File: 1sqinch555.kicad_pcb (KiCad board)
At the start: 2 copper layers, 104.5 x 25 mm, 75 parts, among them J1 Conn_01x01, J10 Conn_01x01, J11 Conn_01x01, J12 Conn_01x01, J13 Conn_01x01, J14 Conn_01x01, J15 Conn_01x01, J16 Conn_01x01, J17 Conn_01x01, J18 Conn_01x01, J19 Conn_01x01, J2 Conn_01x01, J20 Conn_01x01, J21 Conn_01x01, J22 Conn_01x01, J23 Conn_01x01, J24 Conn_01x01, J25 Conn_01x01, J26 Conn_01x01, J27 Conn_01x01, J28 Conn_01x01, J29 Conn_01x01, J3 Conn_01x01, J30 Conn_01x01, J31 Conn_01x01, J32 Conn_01x01, J33 Conn_01x01, J34 Conn_01x01, J35 Conn_01x01, J4 Conn_01x01, J5 Conn_01x01, J6 Conn_01x01, J7 Conn_01x01, J8 Conn_01x01, J9 Conn_01x01, U1 LM555, U2 4020

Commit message: changed 0603 to 0805
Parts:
- added R10: 300, 1sqinch555_fp:R_0805, F.Cu at (137.7, 38.5)
- added R2: 300, 1sqinch555_fp:R_0805, F.Cu at (69.4, 38.5)
- added R3: 300, 1sqinch555_fp:R_0805, F.Cu at (73.8, 38.5)
- added R4: 300, 1sqinch555_fp:R_0805, F.Cu at (84.6, 38.5)
- added R5: 300, 1sqinch555_fp:R_0805, F.Cu at (95.9, 38.5)
- added R6: 300, 1sqinch555_fp:R_0805, F.Cu at (100.3, 38.5)
- added R7: 300, 1sqinch555_fp:R_0805, F.Cu at (111.1, 38.5)
- added R8: 300, 1sqinch555_fp:R_0805, F.Cu at (122.3, 38.5)
- added R9: 300, 1sqinch555_fp:R_0805, F.Cu at (126.9, 38.5)
- C1, C2: footprint 1sqinch555_fp:C_0603 -> 1sqinch555_fp:C_0805
- D1, D10, D11, D12, D13, D14, D15, D16, D17, D18, D19, D2, D20, D21, D22, D23, D24, D25, D26, D27, D3, D4, D5, D6, D7, D8, D9: footprint 1sqinch555_fp:D_0603 -> 1sqinch555_fp:LED-0805
- R1: footprint 1sqinch555_fp:R_0603 -> 1sqinch555_fp:R_0805
- moved J30 1.50 mm to (71.5, 41.0)
- moved J31 1.50 mm to (82.5, 41.0)
- moved J32 1.50 mm to (98.0, 41.0)
- moved J33 1.50 mm to (109.0, 41.0)
- moved J34 1.50 mm to (135.5, 41.0)
- moved J35 1.50 mm to (124.5, 41.0)
- moved C1 0.51 mm to (55.5, 60.6)
- moved R1 0.51 mm to (53.0, 60.6)
- moved D11 0.20 mm to (92.7, 47.5)
- moved D17 0.20 mm to (114.3, 47.5)
- moved D2 0.20 mm to (66.2, 47.5)
- moved D20 0.20 mm to (119.2, 47.5)
- moved D8 0.20 mm to (87.8, 47.5)
- moved D26 0.20 mm to (140.8, 47.5)
- moved D1 0.20 mm to (66.2, 55.5)
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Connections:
- D12 pad 1: /GND2 -> Net-(D12-Pad1)
- D15 pad 1: /GND2 -> Net-(D15-Pad1)
- D18 pad 1: /GND2 -> Net-(D18-Pad1)
- D21 pad 1: /GND3 -> Net-(D21-Pad1)
- D24 pad 1: /GND3 -> Net-(D24-Pad1)
- D27 pad 1: /GND3 -> Net-(D27-Pad1)
- D3 pad 1: /GND1 -> Net-(D3-Pad1)
- D6 pad 1: /GND1 -> Net-(D6-Pad1)
- D9 pad 1: /GND1 -> Net-(D9-Pad1)
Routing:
- net /GND3: track 63.4 -> 0.00 mm
- net /GND1: track 63.4 -> 0.00 mm
- net /GND2: track 63.4 -> 0.00 mm
- net /GND: track 16.4 -> 4.62 mm
- net Net-(D8-Pad1): track 6.30 -> 0.00 mm
- net Net-(D7-Pad1): track 6.30 -> 0.00 mm
- net Net-(D26-Pad1): track 6.30 -> 0.00 mm
- net Net-(D25-Pad1): track 6.30 -> 0.00 mm
- net Net-(D20-Pad1): track 6.30 -> 0.00 mm
- net Net-(D2-Pad1): track 6.30 -> 0.00 mm
- net Net-(D19-Pad1): track 6.30 -> 0.00 mm
- net Net-(D17-Pad1): track 6.30 -> 0.00 mm
- net Net-(D16-Pad1): track 6.30 -> 0.00 mm
- net Net-(D11-Pad1): track 6.30 -> 0.00 mm
- net Net-(D10-Pad1): track 6.30 -> 0.00 mm
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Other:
- outline, holes or cut-outs redrawn

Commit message: layout changes
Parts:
- moved C1 11.0 mm to (46.0, 55.0)
- moved R1 11.0 mm to (43.5, 55.0), turned to 90 degrees
- moved G1 4.73 mm to (36.5, 41.6), turned to 0 degrees
- moved C2 1.04 mm to (57.7, 59.6), turned to 180 degrees
- moved J3 0.83 mm to (51.2, 47.5)
- moved J1 0.81 mm to (60.5, 54.5)
- moved U1 0.80 mm to (56.0, 55.2)
- moved R8 0.11 mm to (122.4, 38.5)
- moved R9 0.11 mm to (126.8, 38.5)
- moved R10 0.11 mm to (137.6, 38.5)
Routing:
- net /GND: track 4.62 -> 66.9 mm, vias 6 -> 7
- net /GND3: track 0.00 -> 41.3 mm, vias 0 -> 1
- net /GND2: track 0.00 -> 41.3 mm, vias 0 -> 1
- net /GND1: track 0.00 -> 41.3 mm, vias 0 -> 1
- net /OUT: track 17.9 -> 28.2 mm
- net /Q13: track 28.2 -> 37.6 mm
- net Net-(D8-Pad1): track 0.00 -> 5.90 mm
- net Net-(D7-Pad1): track 0.00 -> 5.90 mm
- net Net-(D5-Pad1): track 0.00 -> 5.90 mm
- net Net-(D4-Pad1): track 0.00 -> 5.90 mm
- net Net-(D26-Pad1): track 0.00 -> 5.90 mm
- net Net-(D25-Pad1): track 0.00 -> 5.90 mm
- net Net-(D23-Pad1): track 0.00 -> 5.90 mm
- net Net-(D22-Pad1): track 0.00 -> 5.90 mm
- net Net-(D20-Pad1): track 0.00 -> 5.90 mm
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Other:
- outline, holes or cut-outs redrawn
- board text added: "1sqinch555"

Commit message: mods
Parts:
- removed mouse-bite-2.5mm-slot (x6): VAL**, 1sqinch555_fp:mouse-bite-2.5mm-slot
- moved D19 4.50 mm to (114.7, 55.5)
- moved D20 4.50 mm to (114.7, 47.5)
- moved D21 4.50 mm to (114.7, 39.5)
- moved D22 4.50 mm to (125.5, 55.5)
- moved D23 4.50 mm to (125.5, 47.5)
- moved D24 4.50 mm to (125.5, 39.5)
- moved D25 4.50 mm to (136.3, 55.5)
- moved D26 4.50 mm to (136.3, 47.5)
- moved D27 4.50 mm to (136.3, 39.5)
- moved J19 4.50 mm to (114.5, 59.5)
- moved J21 4.50 mm to (125.5, 59.5)
- moved J23 4.50 mm to (136.5, 59.5)
- moved J29 4.50 mm to (131.0, 59.5)
- moved J34 4.50 mm to (131.0, 41.0)
- moved J35 4.50 mm to (120.0, 41.0)
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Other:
- board size 104.5 x 25 mm -> 100 x 25 mm

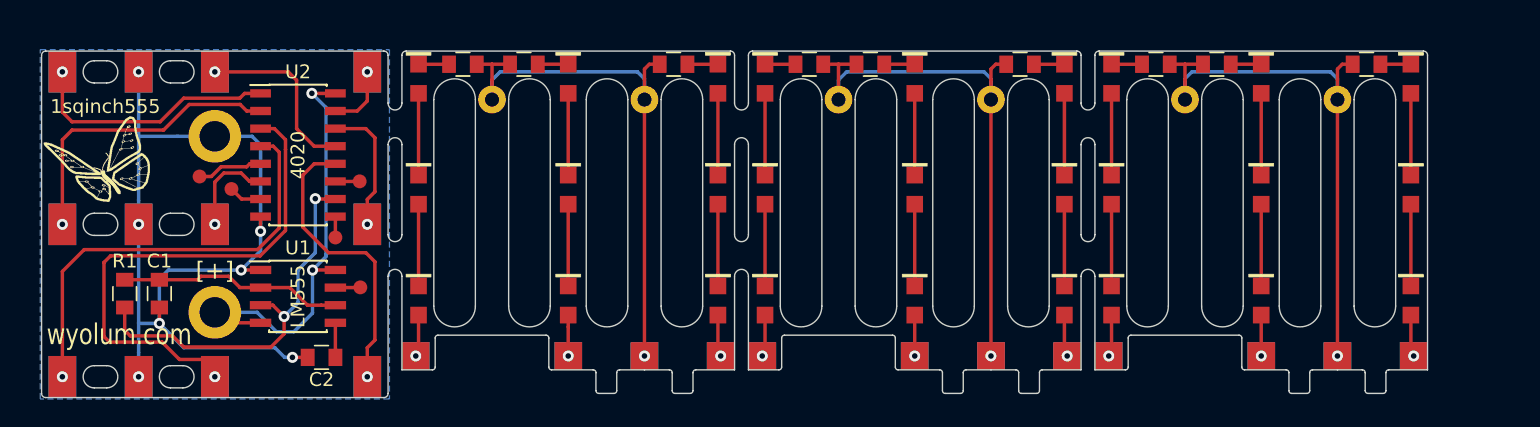
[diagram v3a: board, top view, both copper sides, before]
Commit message: randomizing LEDs
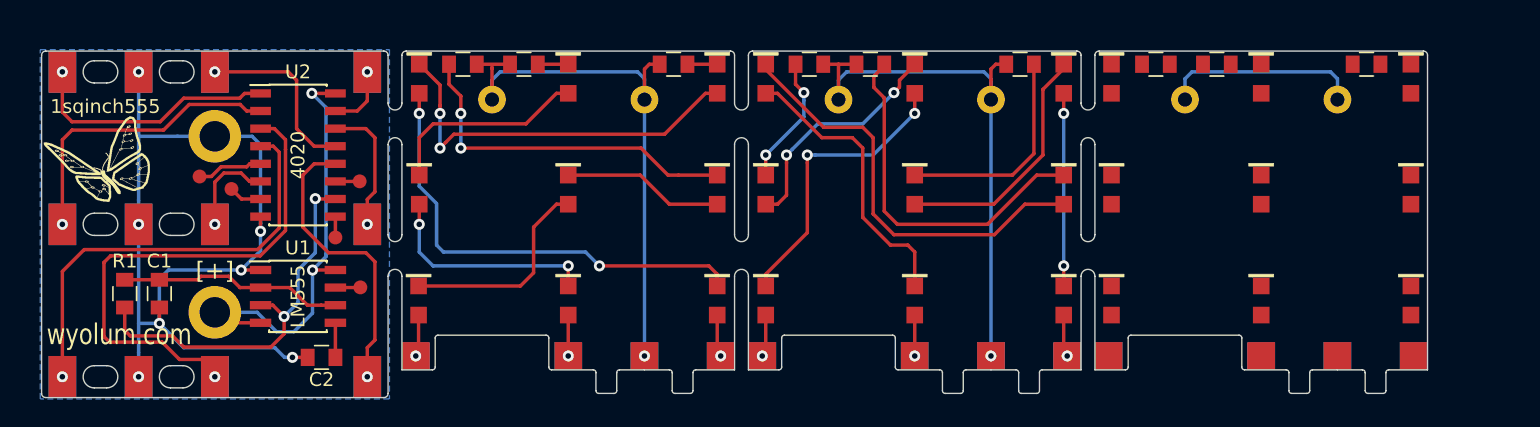
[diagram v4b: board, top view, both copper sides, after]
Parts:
- moved D3 23.0 mm to (86.2, 47.5)
- moved D8 23.0 mm to (64.8, 39.5)
- moved D11 13.4 mm to (100.5, 39.5)
- moved D18 13.4 mm to (100.5, 47.5)
- moved D14 13.4 mm to (89.8, 39.5)
- moved D15 13.4 mm to (111.2, 47.5)
- moved D2 10.8 mm to (75.5, 47.5)
- moved D5 10.8 mm to (64.8, 47.5)
- moved D12 8.00 mm to (89.8, 47.5)
- moved D17 8.00 mm to (111.2, 39.5)
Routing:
- net Net-(D7-Pad1): track 5.90 -> 33.4 mm, vias 0 -> 2
- net /GND3: track 41.3 -> 14.4 mm, vias 1 -> 0
- net Net-(D14-Pad1): track 5.90 -> 30.9 mm
- net Net-(D15-Pad1): track 2.20 -> 26.0 mm
- net Net-(D3-Pad1): track 2.20 -> 25.7 mm, vias 0 -> 2
- net Net-(D8-Pad1): track 5.90 -> 28.3 mm, vias 0 -> 2
- net Net-(D10-Pad1): track 5.90 -> 21.1 mm, vias 0 -> 2
- net Net-(D13-Pad1): track 5.90 -> 20.9 mm
- net Net-(D18-Pad1): track 2.20 -> 15.7 mm
- net Net-(D17-Pad1): track 5.90 -> 17.9 mm
- net Net-(D11-Pad1): track 5.90 -> 17.0 mm, vias 0 -> 2
- net Net-(D4-Pad1): track 5.90 -> 16.1 mm, vias 0 -> 2
- net Net-(D1-Pad1): track 5.90 -> 15.2 mm
- net Net-(D5-Pad1): track 5.90 -> 14.8 mm
- net Net-(D16-Pad1): track 5.90 -> 13.9 mm, vias 0 -> 2
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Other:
- outline, holes or cut-outs redrawn

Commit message: 1mm PCB thickness
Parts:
- added REF**: Unplated_Hole_d1.0mm, 1sqinch555_fp:Unplated_Hole_d1.0mm, F.Cu at (63.0, 51.0)
- added REF**: Unplated_Hole_d1.0mm, 1sqinch555_fp:Unplated_Hole_d1.0mm, F.Cu at (63.0, 57.0)
- added REF**: Unplated_Hole_d1.0mm, 1sqinch555_fp:Unplated_Hole_d1.0mm, F.Cu at (88.0, 39.0)
- added REF**: Unplated_Hole_d1.0mm, 1sqinch555_fp:Unplated_Hole_d1.0mm, F.Cu at (88.0, 41.0)
- added REF**: Unplated_Hole_d1.0mm, 1sqinch555_fp:Unplated_Hole_d1.0mm, F.Cu at (88.0, 43.0)
- added REF**: Unplated_Hole_d1.0mm, 1sqinch555_fp:Unplated_Hole_d1.0mm, F.Cu at (88.0, 45.0)
- added REF**: Unplated_Hole_d1.0mm, 1sqinch555_fp:Unplated_Hole_d1.0mm, F.Cu at (88.0, 47.0)
- added REF**: Unplated_Hole_d1.0mm, 1sqinch555_fp:Unplated_Hole_d1.0mm, F.Cu at (88.0, 49.0)
- added REF**: Unplated_Hole_d1.0mm, 1sqinch555_fp:Unplated_Hole_d1.0mm, F.Cu at (88.0, 51.0)
- added REF**: Unplated_Hole_d1.0mm, 1sqinch555_fp:Unplated_Hole_d1.0mm, F.Cu at (88.0, 53.0)
- added REF**: Unplated_Hole_d1.0mm, 1sqinch555_fp:Unplated_Hole_d1.0mm, F.Cu at (88.0, 55.0)
- added REF**: Unplated_Hole_d1.0mm, 1sqinch555_fp:Unplated_Hole_d1.0mm, F.Cu at (63.0, 39.0)
- added REF**: Unplated_Hole_d1.0mm, 1sqinch555_fp:Unplated_Hole_d1.0mm, F.Cu at (88.0, 57.0)
- added REF**: Unplated_Hole_d1.0mm, 1sqinch555_fp:Unplated_Hole_d1.0mm, F.Cu at (113.0, 39.0)
- added REF**: Unplated_Hole_d1.0mm, 1sqinch555_fp:Unplated_Hole_d1.0mm, F.Cu at (113.0, 41.0)
- added REF**: Unplated_Hole_d1.0mm, 1sqinch555_fp:Unplated_Hole_d1.0mm, F.Cu at (113.0, 43.0)
- added REF**: Unplated_Hole_d1.0mm, 1sqinch555_fp:Unplated_Hole_d1.0mm, F.Cu at (113.0, 45.0)
- added REF**: Unplated_Hole_d1.0mm, 1sqinch555_fp:Unplated_Hole_d1.0mm, F.Cu at (113.0, 47.0)
- added REF**: Unplated_Hole_d1.0mm, 1sqinch555_fp:Unplated_Hole_d1.0mm, F.Cu at (113.0, 49.0)
- added REF**: Unplated_Hole_d1.0mm, 1sqinch555_fp:Unplated_Hole_d1.0mm, F.Cu at (113.0, 51.0)
- added REF**: Unplated_Hole_d1.0mm, 1sqinch555_fp:Unplated_Hole_d1.0mm, F.Cu at (113.0, 53.0)
- added REF**: Unplated_Hole_d1.0mm, 1sqinch555_fp:Unplated_Hole_d1.0mm, F.Cu at (113.0, 55.0)
- added REF**: Unplated_Hole_d1.0mm, 1sqinch555_fp:Unplated_Hole_d1.0mm, F.Cu at (63.0, 41.0)
- added REF**: Unplated_Hole_d1.0mm, 1sqinch555_fp:Unplated_Hole_d1.0mm, F.Cu at (113.0, 57.0)
- added REF**: Unplated_Hole_d1.0mm, 1sqinch555_fp:Unplated_Hole_d1.0mm, F.Cu at (63.0, 43.0)
- added REF**: Unplated_Hole_d1.0mm, 1sqinch555_fp:Unplated_Hole_d1.0mm, F.Cu at (63.0, 45.0)
- added REF**: Unplated_Hole_d1.0mm, 1sqinch555_fp:Unplated_Hole_d1.0mm, F.Cu at (63.0, 47.0)
- added REF**: Unplated_Hole_d1.0mm, 1sqinch555_fp:Unplated_Hole_d1.0mm, F.Cu at (63.0, 49.0)
- added REF**: Unplated_Hole_d1.0mm, 1sqinch555_fp:Unplated_Hole_d1.0mm, F.Cu at (63.0, 53.0)
- added REF**: Unplated_Hole_d1.0mm, 1sqinch555_fp:Unplated_Hole_d1.0mm, F.Cu at (63.0, 55.0)
- moved D20 23.0 mm to (136.2, 39.5)
- moved D26 21.6 mm to (114.8, 47.5)
- moved R2 17.1 mm to (67.2, 55.5), turned to 270 degrees
- moved R3 17.1 mm to (73.0, 55.5), turned to 270 degrees
- moved R6 17.1 mm to (98.0, 55.5), turned to 270 degrees
- moved R9 17.1 mm to (123.0, 55.5), turned to 270 degrees
- moved R10 17.1 mm to (133.8, 55.5), turned to 270 degrees
- moved R4 17.1 mm to (83.8, 55.5), turned to 270 degrees
- moved R5 17.1 mm to (92.2, 55.5), turned to 270 degrees
- moved R7 17.1 mm to (108.8, 55.5), turned to 270 degrees
- moved R8 17.1 mm to (117.2, 55.5), turned to 270 degrees
- moved D21 13.4 mm to (125.5, 47.5)
- moved D27 10.8 mm to (125.5, 39.5)
- moved D23 10.8 mm to (136.2, 47.5)
- moved D24 10.8 mm to (114.8, 39.5)
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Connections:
- D1 pad 2: /10 -> Net-(D1-Pad2)
- D10 pad 2: /9 -> Net-(D10-Pad2)
- D12 pad 1: Net-(D12-Pad1) -> /GND2
- D13 pad 2: /6 -> Net-(D13-Pad2)
- D15 pad 1: Net-(D15-Pad1) -> /GND2
- D16 pad 2: /12 -> Net-(D16-Pad2)
- D18 pad 1: Net-(D18-Pad1) -> /GND2
- D19 pad 2: /8 -> Net-(D19-Pad2)
- D21 pad 1: Net-(D21-Pad1) -> /GND3
- D22 pad 2: /13 -> Net-(D22-Pad2)
- D24 pad 1: Net-(D24-Pad1) -> /GND3
- D25 pad 2: /5 -> Net-(D25-Pad2)
- D27 pad 1: Net-(D27-Pad1) -> /GND3
- D3 pad 1: Net-(D3-Pad1) -> /GND1
- D4 pad 2: /7 -> Net-(D4-Pad2)
- D6 pad 1: Net-(D6-Pad1) -> /GND1
- D7 pad 2: /11 -> Net-(D7-Pad2)
- D9 pad 1: Net-(D9-Pad1) -> /GND1
- R10 pad 1: /GND3 -> Net-(D25-Pad2)
- R10 pad 2: Net-(D27-Pad1) -> /5
- R2 pad 1: /GND1 -> Net-(D1-Pad2)
- R2 pad 2: Net-(D3-Pad1) -> /10
- R3 pad 1: /GND1 -> Net-(D4-Pad2)
- R3 pad 2: Net-(D6-Pad1) -> /7
- R4 pad 1: /GND1 -> Net-(D7-Pad2)
- R4 pad 2: Net-(D9-Pad1) -> /11
- R5 pad 1: /GND2 -> Net-(D10-Pad2)
- R5 pad 2: Net-(D12-Pad1) -> /9
- R6 pad 1: /GND2 -> Net-(D13-Pad2)
- R6 pad 2: Net-(D15-Pad1) -> /6
- R7 pad 1: /GND2 -> Net-(D16-Pad2)
- R7 pad 2: Net-(D18-Pad1) -> /12
- R8 pad 1: /GND3 -> Net-(D19-Pad2)
- R8 pad 2: Net-(D21-Pad1) -> /8
- R9 pad 1: /GND3 -> Net-(D22-Pad2)
- R9 pad 2: Net-(D24-Pad1) -> /13
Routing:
- net /GND3: track 14.4 -> 56.5 mm, vias 0 -> 1
- net Net-(D23-Pad1): track 0.00 -> 35.1 mm, vias 0 -> 2
- net Net-(D19-Pad1): track 0.00 -> 32.9 mm
- net /GND2: track 41.3 -> 71.0 mm
- net Net-(D25-Pad1): track 0.00 -> 28.3 mm, vias 0 -> 2
- net Net-(D15-Pad1): track 26.0 -> 0.00 mm
- net Net-(D3-Pad1): track 25.7 -> 0.00 mm, vias 2 -> 0
- net Net-(D20-Pad1): track 0.00 -> 19.9 mm
- net Net-(D26-Pad1): track 0.00 -> 18.4 mm, vias 0 -> 2
- net Net-(D18-Pad1): track 15.7 -> 0.00 mm
- net Net-(D22-Pad1): track 0.00 -> 15.0 mm
- net /GND1: track 41.2 -> 54.5 mm, vias 1 -> 2
- net Net-(D12-Pad1): track 9.39 -> 0.00 mm, vias 2 -> 0
- net /8: track 0.00 -> 5.16 mm, vias 0 -> 1
- net /5: track 0.00 -> 5.16 mm, vias 0 -> 1
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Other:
- outline, holes or cut-outs redrawn
